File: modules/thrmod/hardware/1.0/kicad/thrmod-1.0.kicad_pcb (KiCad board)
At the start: 2 copper layers, 75 x 75 mm, 50 parts, among them J1 Screw_Terminal_01x02, J2 Screw_Terminal_01x02, J3 SWITCHES, J4 CAN, K1 FINDER-32.21-x300, K2 FINDER-32.21-x300, Q1 NTE123A, Q2 NTE123A, SW1 SCR, SW2 MODE, SW3 INSTANCE, U1 PDJR_Teensy_3.2, U2 MCP2551-I-P, U3 TMR-1-1211, U4 CNY74-2H

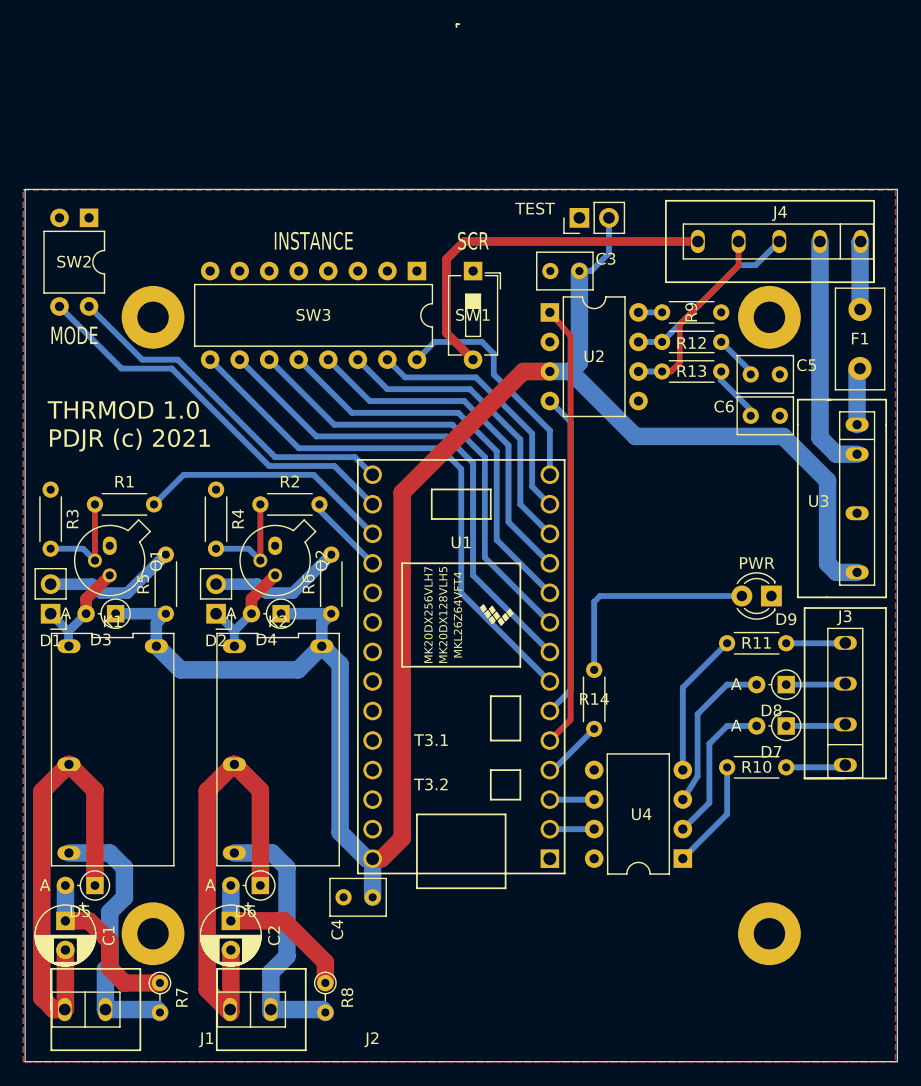
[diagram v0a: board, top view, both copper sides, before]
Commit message: Add thruster firmware
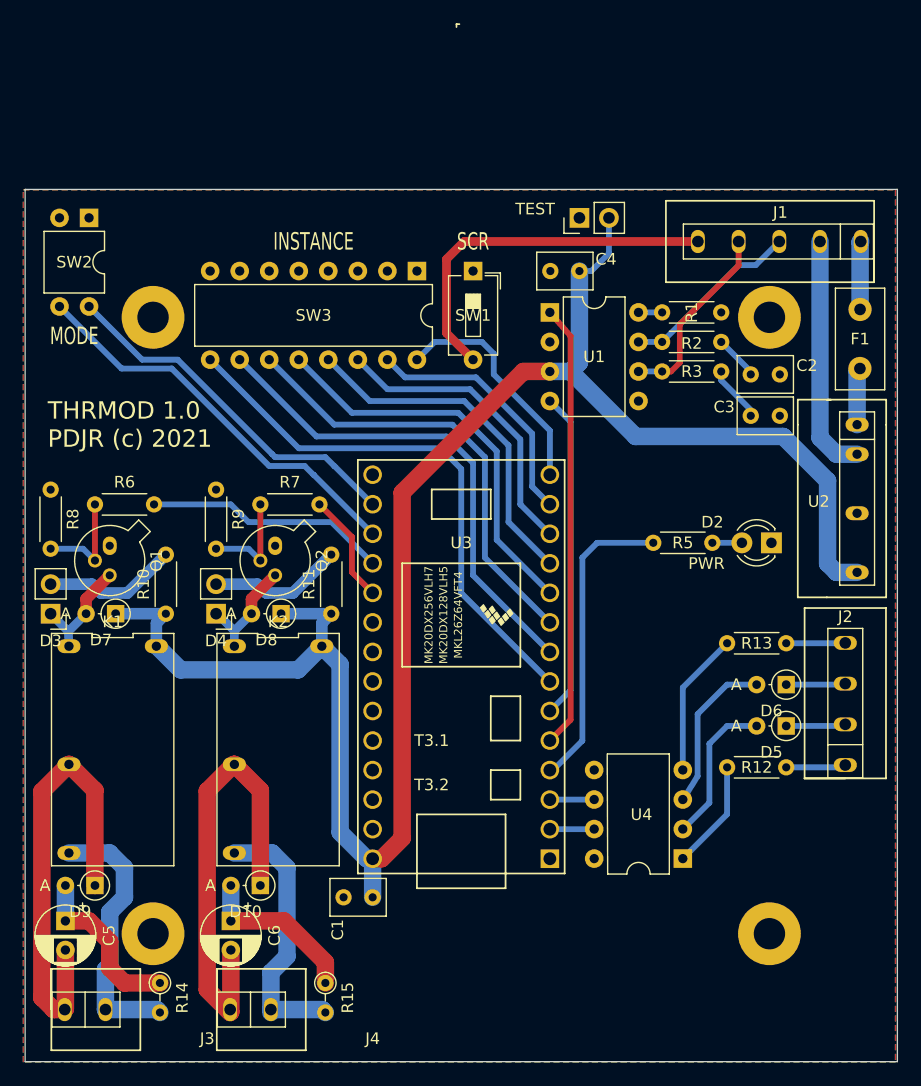
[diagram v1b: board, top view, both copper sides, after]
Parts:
- moved R5 16.8 mm to (190.2, 117.3), turned to 0 degrees
- moved D2 4.57 mm to (200.3, 117.3)
- renumbered C4 to C1, C5 to C2, C6 to C3, C3 to C4, C1 to C5, C2 to C6, D6 to D10, D9 to D2, D1 to D3, D2 to D4, D7 to D5, D8 to D6, D3 to D7, D4 to D8, D5 to D9, J4 to J1, J3 to J2, J1 to J3, J2 to J4, R9 to R1, R5 to R10, R6 to R11, R10 to R12, R11 to R13, R7 to R14, R8 to R15, R12 to R2, R13 to R3, R14 to R5, R1 to R6, R2 to R7, R3 to R8, R4 to R9, U2 to U1, U3 to U2, U1 to U3
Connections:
- net /PORT_G renamed /PS_G
- net /PORT_P renamed /PS_P
- net /STARBOARD_G renamed /SB_G
- net /STARBOARD_P renamed /SB_P
- net /THRUST_PORT renamed /PS_CMD
- net /THRUST_STARBOARD renamed /SB_CMD
- R6 pad 2: /RELAY_PORT -> /PS_RLY
- R7 pad 2: /RELAY_STARBOARD -> /SB_RLY
- U3 pad 15: /MODE_SEL -> (no net)
- U3 pad 16: /COMMON -> /MODE_SEL
- U3 pad 17: /RELAY_PORT -> /COMMON
- U3 pad 18: /RELAY_STARBOARD -> /PS_RLY
- U3 pad 19: (no net) -> /SB_RLY
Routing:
- net /RELAY_PORT: track 21.9 -> 0.00 mm
- net /LED_PWR: track 5.44 -> 26.4 mm
- net /PS_RLY: track 0.00 -> 20.9 mm
- net Net-(D2-Pad2): track 18.8 -> 2.54 mm
- net /SB_RLY: track 0.00 -> 9.50 mm
- net /RELAY_STARBOARD: track 6.96 -> 0.00 mm
- net /MODE_SEL: track 30.4 -> 31.4 mm
- net /COMMON: track 34.0 -> 35.0 mm
